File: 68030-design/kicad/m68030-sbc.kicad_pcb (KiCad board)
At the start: 4 copper layers, 220 x 175 mm, 279 parts, among them J1 SIMM-72 socket, J10 DIN41612-C-96, J11 LA1 A31-A0, J12 LA2 D31-D0, J13 LA3 control, J2 9-24V DC, J3 5V_BENCH, J4 JTAG (ATDH1150USB), J5 JTAG U4 (ATDH1150USB), J6 IDE 40-pin, J7 TTL-232, J8 TTL-232, J9 SPI NIC, Q1 SUD50P04-08, SW1 WARM_RESET, SW2 NMI, SW3 COLD_RESET, U1 MC68030RC33C, U10 74ACT244, U11 SN74ACT245DW, U12 SN74ACT245DW, U13 SN74ACT245DW, U14 SN74ACT244DW, U15 SN74ACT244DW, U16 SN74ACT244DW, U17 SN74ACT244DW, U18 SN74ACT245DW, U19 SN74ACT245DW, U2 MC68882FN33A, U20 SN74ACT245DW, U21 SN74ACT245DW, U22 SN74LVC125ADR, U23 DS3234S#, U27 TPS3808G50DBVR, U3 ATF1508AS-7JX84, U4 ATF1508AS-7JX84, U5 SST39SF040-70-4C-NHE, U6 SC26C92A1A, U7 TPS3702CX50DDCR, U8 LM2678S-5.0, U9 AMS1117-3.3, X1 25.000MHz, X2 50.000MHz, X3 FPU osc (DNP), Y1 3.6864MHz

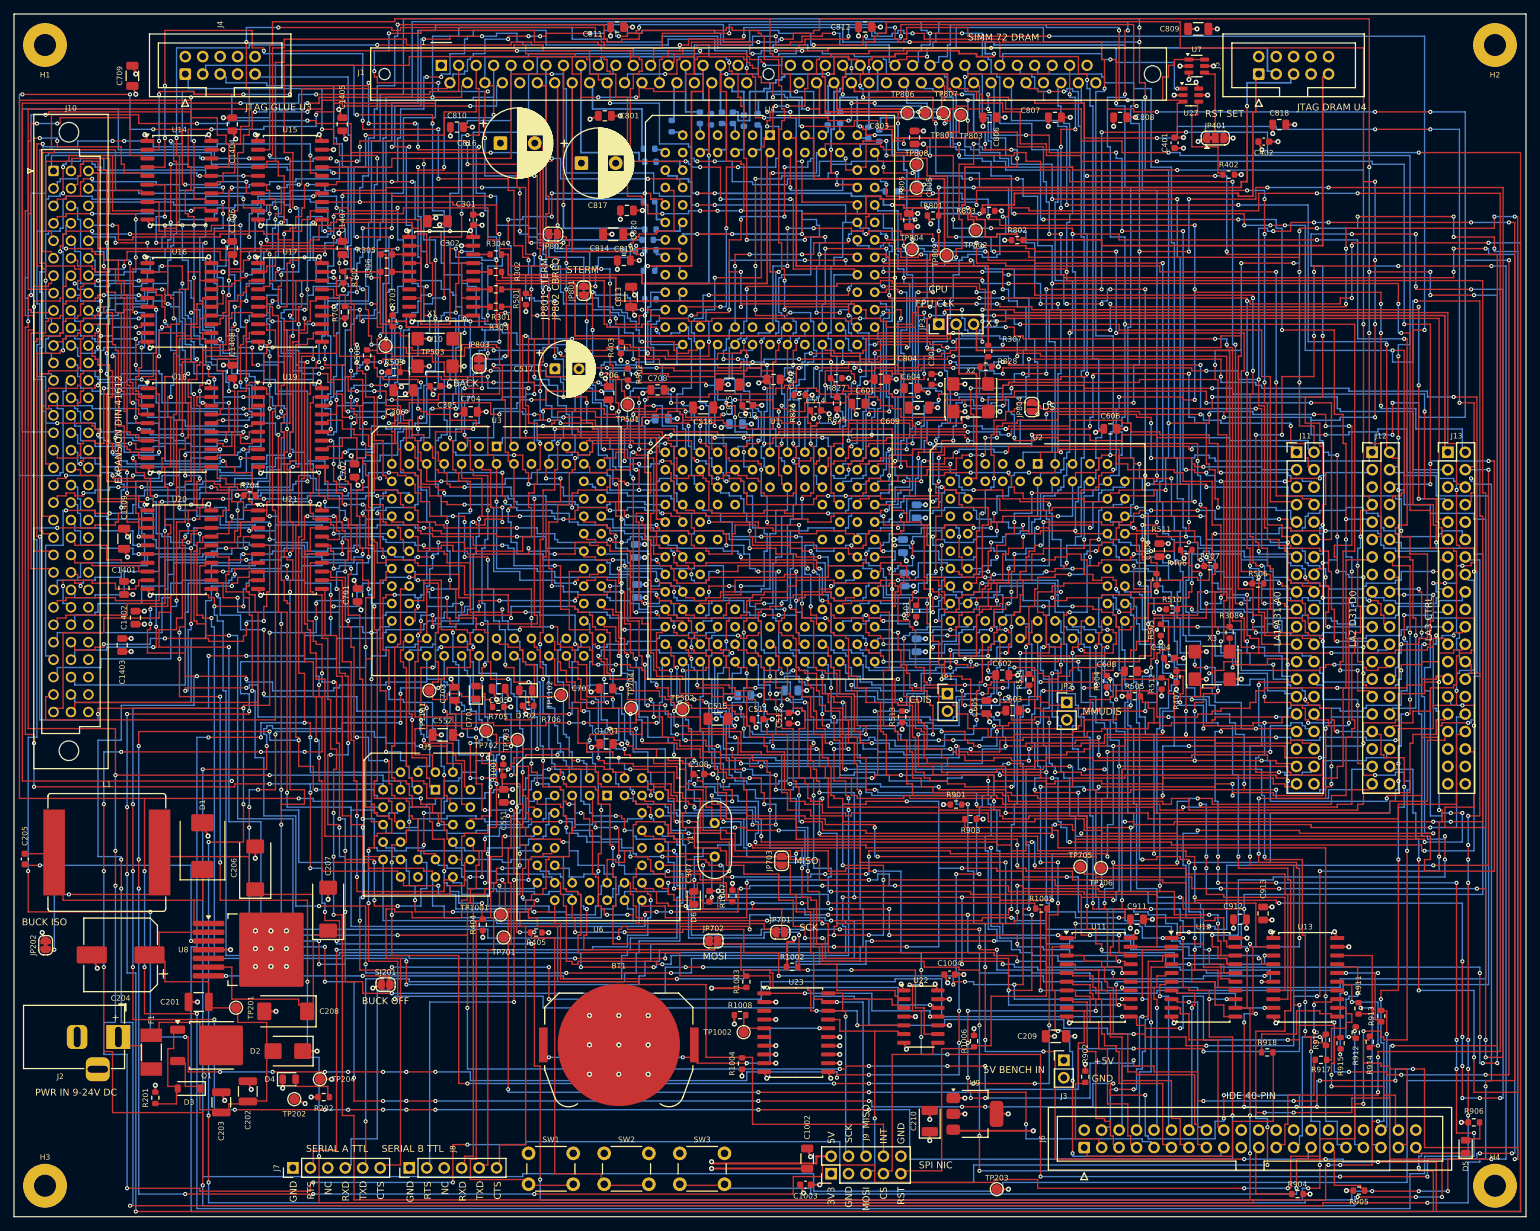
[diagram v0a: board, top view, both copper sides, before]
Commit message: PCB: 45-degree chamfers and de-hitch pull-tight pass
Two cleanup passes on the routed 4-layer board. Placement, vias and layers are
unchanged; only the F.Cu/B.Cu signal tracks were edited.

45-degree chamfer pass (kicad/tools/route/chamfer45/):
- 14,403 corners chamfered at the largest size the clearance allows (0.1-8.9 mm).
  90-degree bends 14,456 -> 43 (14 on a via, 25 inside a same-net pad,
  4 with no room).
- Signal track 53.84 -> 49.87 m. Vias 2365, unchanged. No net got longer.

De-hitch / pull-tight pass (kicad/tools/route/dehitch/):
- Each path between pads, vias and T-junctions is rebuilt with the fewest
  octilinear segments (bends <= 45 degrees). Small jogs are removed by shifting
  a leg sideways. New segments keep >= 0.20 mm clearance; where a gap was already
  tighter, a path may not get more sub-0.2 mm gaps or a smaller worst gap.
- Segments 18,293 -> 13,407. Jogs < 1 mm 5,694 -> 2,217 (all sizes 8,400 -> 4,457).
  Bends 15,211 -> 10,267. Length 49.866 -> 49.628 m. Vias 2365.
- Clearance: segments with a gap < 0.20 mm 799 -> 674 (0.16-0.18 mm: 129 -> 112);
  track-to-object pairs < 0.20 mm 1,030 -> 867. Nothing is below 0.16 mm.
- No SI net got longer (RAS0_n 24.54 -> 24.15 mm, the rest unchanged).
- Remaining ~2,175 jogs under 1 mm: 1,008 would need < 0.20 mm clearance,
  703 would need a > 45-degree bend, 340 sit at a fixed via, 124 at a
  multi-track pad or T-junction. Most are lane changes in dense buses.

Result: pcb sha1 e88d2ee4. 100 % routed, DRC 0 errors, 0 unconnected,
parity 0, ERC 0/0. .kicad_pro unchanged.
Renders: renders/m68030-sbc-45deg-*.png, renders/m68030-sbc-dehitch-*.png
(the zoom images show the same window, for comparison).
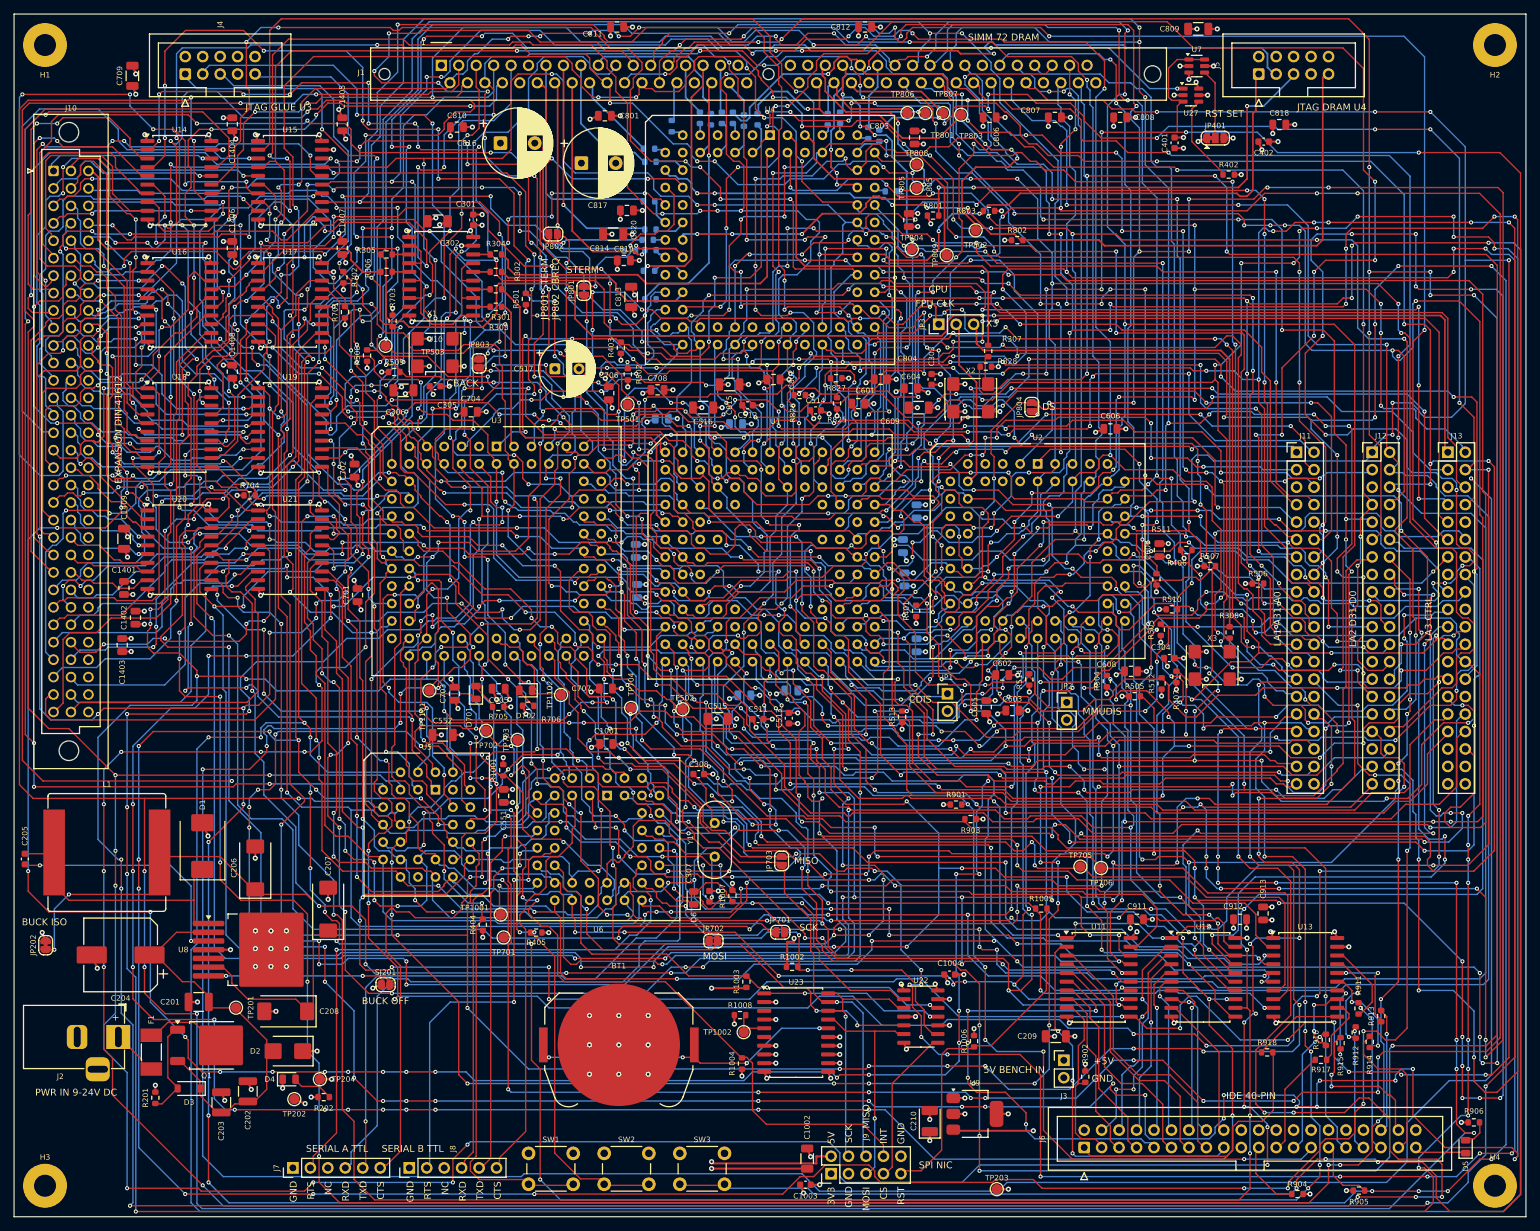
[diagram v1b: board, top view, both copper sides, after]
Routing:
- net /D21: track 759.9 -> 699.4 mm
- net /D12: track 736.2 -> 679.1 mm
- net /R_W: track 664.2 -> 608.3 mm
- net /D20: track 585.9 -> 530.6 mm
- net /D2: track 465.2 -> 412.5 mm
- net /D18: track 778.5 -> 728.9 mm
- net /D17: track 562.6 -> 513.4 mm
- net /D7: track 435.6 -> 386.8 mm
- net /D5: track 663.8 -> 615.1 mm
- net /A8: track 855.1 -> 806.9 mm
- net /A1: track 445.8 -> 399.0 mm
- net /D19: track 550.3 -> 504.9 mm
- net /A6: track 737.9 -> 693.0 mm
- net /A2: track 418.3 -> 373.6 mm
- net /A17: track 843.7 -> 800.3 mm
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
